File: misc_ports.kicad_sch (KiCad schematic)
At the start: 36 parts, among them J10 Molex 46765-2301, J3 Wuerth_7499010121A, J7 QMTECH JTAG, J8 RTC, J9 1140084168 microSD Card Slot, P1 Full-side CD Card Slot, U12 DP83826, U13 74LVC374, U14 PTN3363BSMP

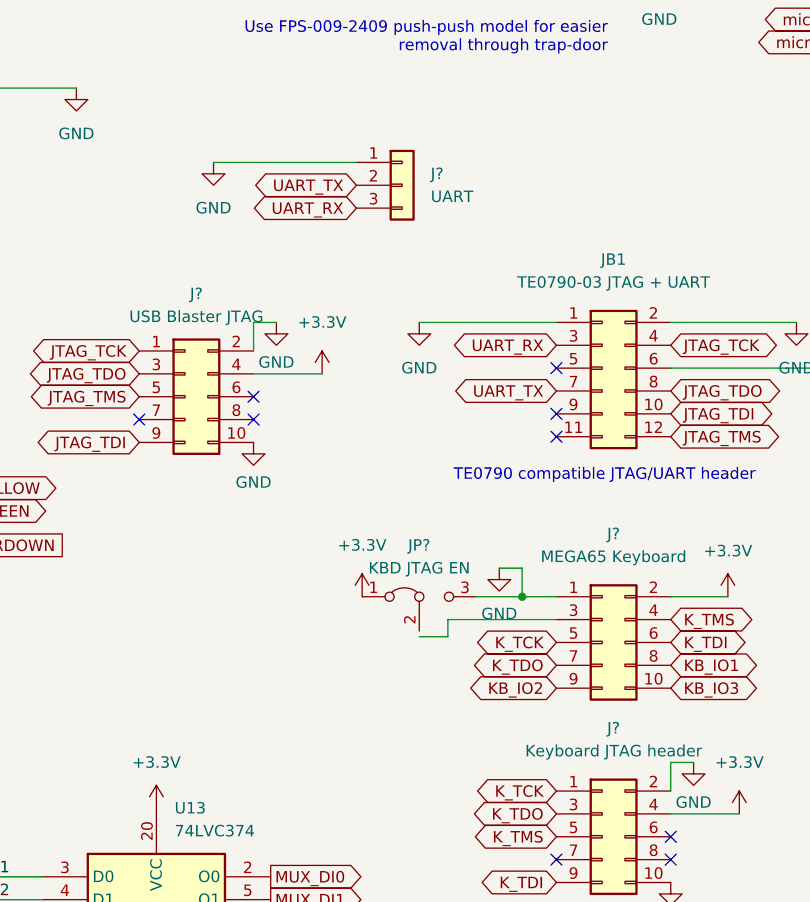
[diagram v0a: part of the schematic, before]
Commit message: place some mounting holes and reset button #3
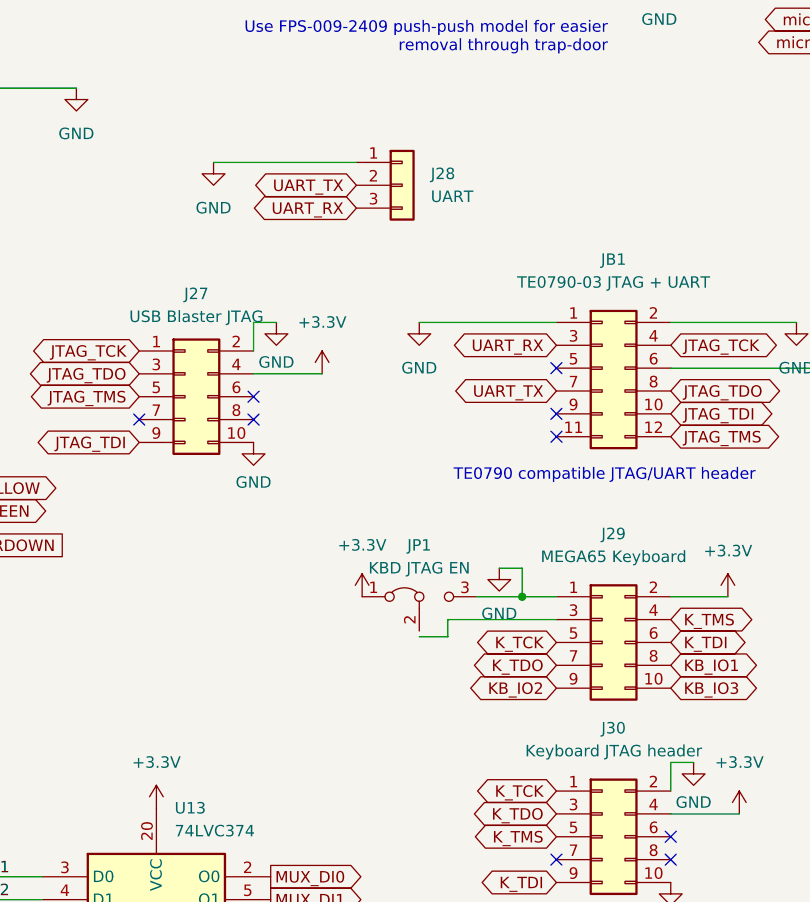
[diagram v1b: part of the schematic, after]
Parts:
- gave numbers to parts that had none: 5
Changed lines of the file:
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@@
   (symbol (lib_id "Connector_Generic:Conn_01x03") (at 128.905 80.645 0) (unit 1)
     (in_bom yes) (on_board yes) (fields_autoplaced)
-    (property "Reference" "J?" (id 0) (at 132.08 79.3749 0)
+    (property "Reference" "J28" (id 0) (at 132.08 79.3749 0)
       (effects (font (size 1.27 1.27)) (justify left))
     )
@@
   (symbol (lib_id "power:GND") (at 112.395 109.22 0) (unit 1)
     (in_bom yes) (on_board yes) (fields_autoplaced)
-    (property "Reference" "#PWR?" (id 0) (at 112.395 115.57 0)
+    (property "Reference" "#PWR0299" (id 0) (at 112.395 115.57 0)
       (effects (font (size 1.27 1.27)) hide)
     )
@@
   (symbol (lib_id "power:+3.3V") (at 165.1 126.365 0) (unit 1)
     (in_bom yes) (on_board yes) (fields_autoplaced)
-    (property "Reference" "#PWR?" (id 0) (at 165.1 130.175 0)
+    (property "Reference" "#PWR0300" (id 0) (at 165.1 130.175 0)
       (effects (font (size 1.27 1.27)) hide)
     )
@@
   (symbol (lib_id "Connector_Generic:Conn_02x05_Odd_Even") (at 151.13 153.035 0) (unit 1)
     (in_bom yes) (on_board yes) (fields_autoplaced)
-    (property "Reference" "J?" (id 0) (at 152.4 140.97 0))
+    (property "Reference" "J30" (id 0) (at 152.4 140.97 0))
     (property "Value" "Keyboard JTAG header" (id 1) (at 152.4 143.51 0))
     (property "Footprint" "Connector_PinHeader_2.54mm:PinHeader_2x05_P2.54mm_Vertical" (id 2) (at 151.13 153.035 0)
@@
   (symbol (lib_id "Connector_Generic:Conn_02x05_Odd_Even") (at 151.13 131.445 0) (unit 1)
     (in_bom yes) (on_board yes) (fields_autoplaced)
-    (property "Reference" "J?" (id 0) (at 152.4 119.38 0))
+    (property "Reference" "J29" (id 0) (at 152.4 119.38 0))
     (property "Value" "MEGA65 Keyboard" (id 1) (at 152.4 121.92 0))
     (property "Footprint" "" (id 2) (at 151.13 131.445 0)
@@
   (symbol (lib_id "Jumper:Jumper_3_Bridged12") (at 130.81 126.365 0) (unit 1)
     (in_bom yes) (on_board yes) (fields_autoplaced)
-    (property "Reference" "JP?" (id 0) (at 130.81 120.65 0))
+    (property "Reference" "JP1" (id 0) (at 130.81 120.65 0))
     (property "Value" "KBD JTAG EN" (id 1) (at 130.81 123.19 0))
     (property "Footprint" "Connector_PinHeader_2.54mm:PinHeader_1x03_P2.54mm_Vertical" (id 2) (at 130.81 126.365 0)
@@
   (symbol (lib_id "power:+3.3V") (at 166.37 150.495 0) (unit 1)
     (in_bom yes) (on_board yes) (fields_autoplaced)
-    (property "Reference" "#PWR?" (id 0) (at 166.37 154.305 0)
+    (property "Reference" "#PWR0303" (id 0) (at 166.37 154.305 0)
       (effects (font (size 1.27 1.27)) hide)
     )
@@
   (symbol (lib_id "Connector_Generic:Conn_02x05_Odd_Even") (at 104.775 104.14 0) (unit 1)
     (in_bom yes) (on_board yes) (fields_autoplaced)
-    (property "Reference" "J?" (id 0) (at 106.045 92.71 0))
+    (property "Reference" "J27" (id 0) (at 106.045 92.71 0))
     (property "Value" "USB Blaster JTAG" (id 1) (at 106.045 95.25 0))
     (property "Footprint" "Connector_PinHeader_2.54mm:PinHeader_2x05_P2.54mm_Vertical" (id 2) (at 104.775 104.14 0)
@@
   (symbol (lib_id "power:GND") (at 161.29 144.78 0) (unit 1)
     (in_bom yes) (on_board yes) (fields_autoplaced)
-    (property "Reference" "#PWR?" (id 0) (at 161.29 151.13 0)
+    (property "Reference" "#PWR0301" (id 0) (at 161.29 151.13 0)
       (effects (font (size 1.27 1.27)) hide)
     )
@@
   (symbol (lib_id "power:GND") (at 114.935 95.885 0) (unit 1)
     (in_bom yes) (on_board yes) (fields_autoplaced)
-    (property "Reference" "#PWR?" (id 0) (at 114.935 102.235 0)
+    (property "Reference" "#PWR0296" (id 0) (at 114.935 102.235 0)
       (effects (font (size 1.27 1.27)) hide)
     )
@@
   (symbol (lib_id "power:GND") (at 107.95 78.105 0) (unit 1)
     (in_bom yes) (on_board yes) (fields_autoplaced)
-    (property "Reference" "#PWR?" (id 0) (at 107.95 84.455 0)
+    (property "Reference" "#PWR0294" (id 0) (at 107.95 84.455 0)
       (effects (font (size 1.27 1.27)) hide)
     )
@@
   (symbol (lib_id "power:+3.3V") (at 124.46 126.365 0) (unit 1)
     (in_bom yes) (on_board yes) (fields_autoplaced)
-    (property "Reference" "#PWR?" (id 0) (at 124.46 130.175 0)
+    (property "Reference" "#PWR0297" (id 0) (at 124.46 130.175 0)
       (effects (font (size 1.27 1.27)) hide)
     )
@@
   (symbol (lib_id "power:+3.3V") (at 120.015 101.6 0) (unit 1)
     (in_bom yes) (on_board yes) (fields_autoplaced)
-    (property "Reference" "#PWR?" (id 0) (at 120.015 105.41 0)
+    (property "Reference" "#PWR0295" (id 0) (at 120.015 105.41 0)
       (effects (font (size 1.27 1.27)) hide)
     )
@@
   (symbol (lib_id "power:GND") (at 158.75 158.115 0) (unit 1)
     (in_bom yes) (on_board yes) (fields_autoplaced)
-    (property "Reference" "#PWR?" (id 0) (at 158.75 164.465 0)
+    (property "Reference" "#PWR0302" (id 0) (at 158.75 164.465 0)
       (effects (font (size 1.27 1.27)) hide)
     )
@@
   (symbol (lib_id "power:GND") (at 139.7 123.19 0) (unit 1)
     (in_bom yes) (on_board yes) (fields_autoplaced)
-    (property "Reference" "#PWR?" (id 0) (at 139.7 129.54 0)
-      (effects (font (size 1.27 1.27)) hide)
-    )
+    (property "Reference" "#PWR0298" (id 0) (at 139.7 129.54 0)
+      (effects (font (size 1.27 1.27)) hide)
+    )

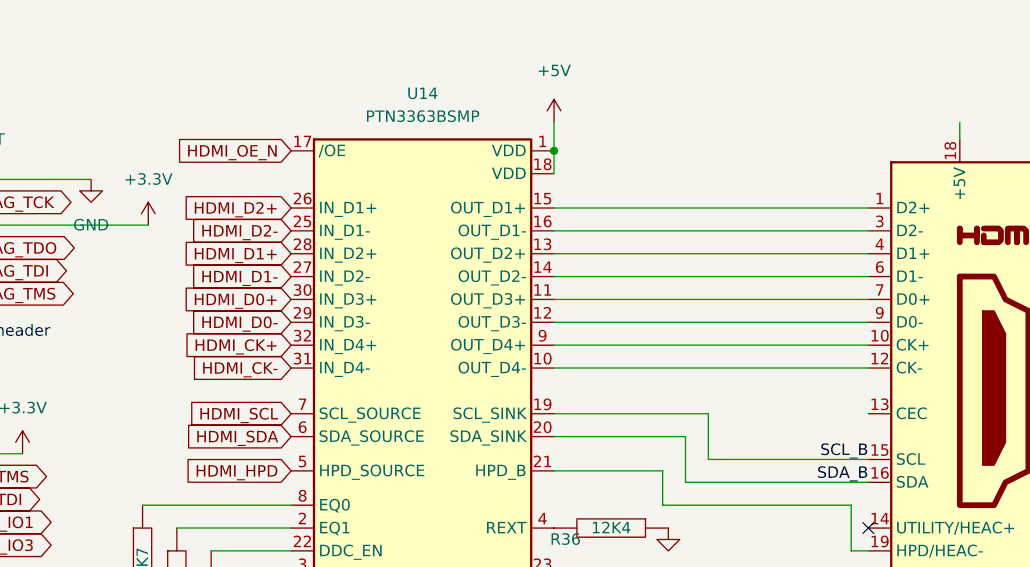
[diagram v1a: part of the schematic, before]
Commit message: rearrange FPGA board connectors to detangle. Begin routing HDMI
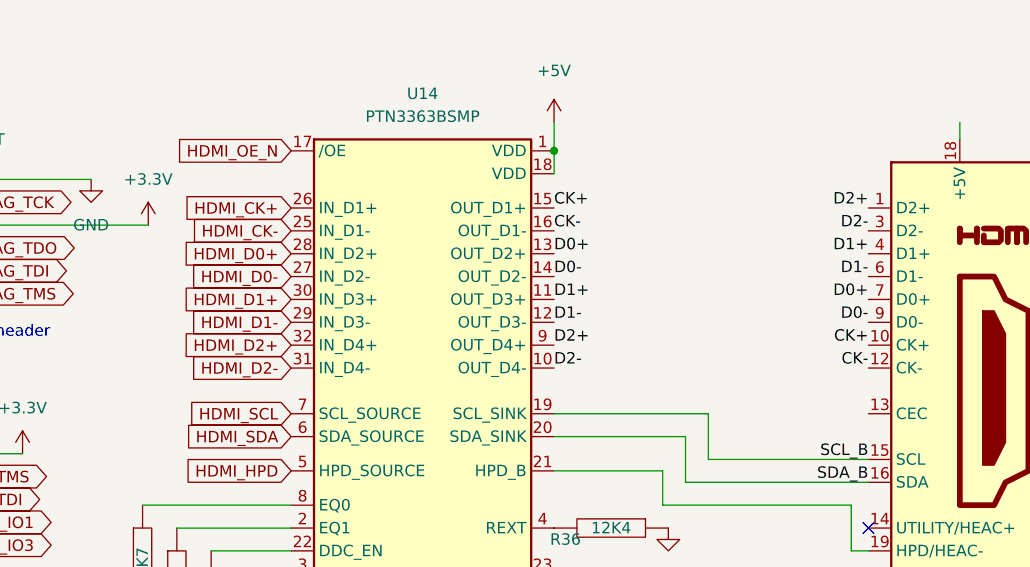
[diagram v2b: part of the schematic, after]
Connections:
- net HDMI_CK+: now also U14.26 (IN_D1+); no longer U14.32 (IN_D4+)
- net HDMI_CK-: now also U14.25 (IN_D1-); no longer U14.31 (IN_D4-)
- net HDMI_D0+: now also U14.28 (IN_D2+); no longer U14.30 (IN_D3+)
- net HDMI_D0-: now also U14.27 (IN_D2-); no longer U14.29 (IN_D3-)
- net HDMI_D1+: now also U14.30 (IN_D3+); no longer U14.28 (IN_D2+)
- net HDMI_D1-: now also U14.29 (IN_D3-); no longer U14.27 (IN_D2-)
- net HDMI_D2+: now also U14.32 (IN_D4+); no longer U14.26 (IN_D1+)
- net HDMI_D2-: now also U14.31 (IN_D4-); no longer U14.25 (IN_D1-)
- net CK+: now reaches U14.15 (OUT_D1+)
- net CK+: now also J10.10 (CK+); no longer J10.1 (D2+)
- net D2+: now reaches U14.9 (OUT_D4+)
- net D2+: now also J10.1 (D2+); no longer J10.10 (CK+)
- net CK-: now reaches J10.12 (CK-)
- net CK-: now also U14.16 (OUT_D1-); no longer U14.10 (OUT_D4-)
- net D2-: now reaches J10.3 (D2-)
- net D2-: now also U14.10 (OUT_D4-); no longer U14.16 (OUT_D1-)
- net D0+: now reaches U14.13 (OUT_D2+)
- net D0+: now also J10.7 (D0+); no longer J10.4 (D1+)
- net D0-: now reaches U14.14 (OUT_D2-)
- net D0-: now also J10.9 (D0-); no longer J10.6 (D1-)
- net D1+: now reaches U14.11 (OUT_D3+)
- net D1+: now also J10.4 (D1+); no longer J10.7 (D0+)
- net D1-: now reaches U14.12 (OUT_D3-)
- net D1-: now also J10.6 (D1-); no longer J10.9 (D0-)

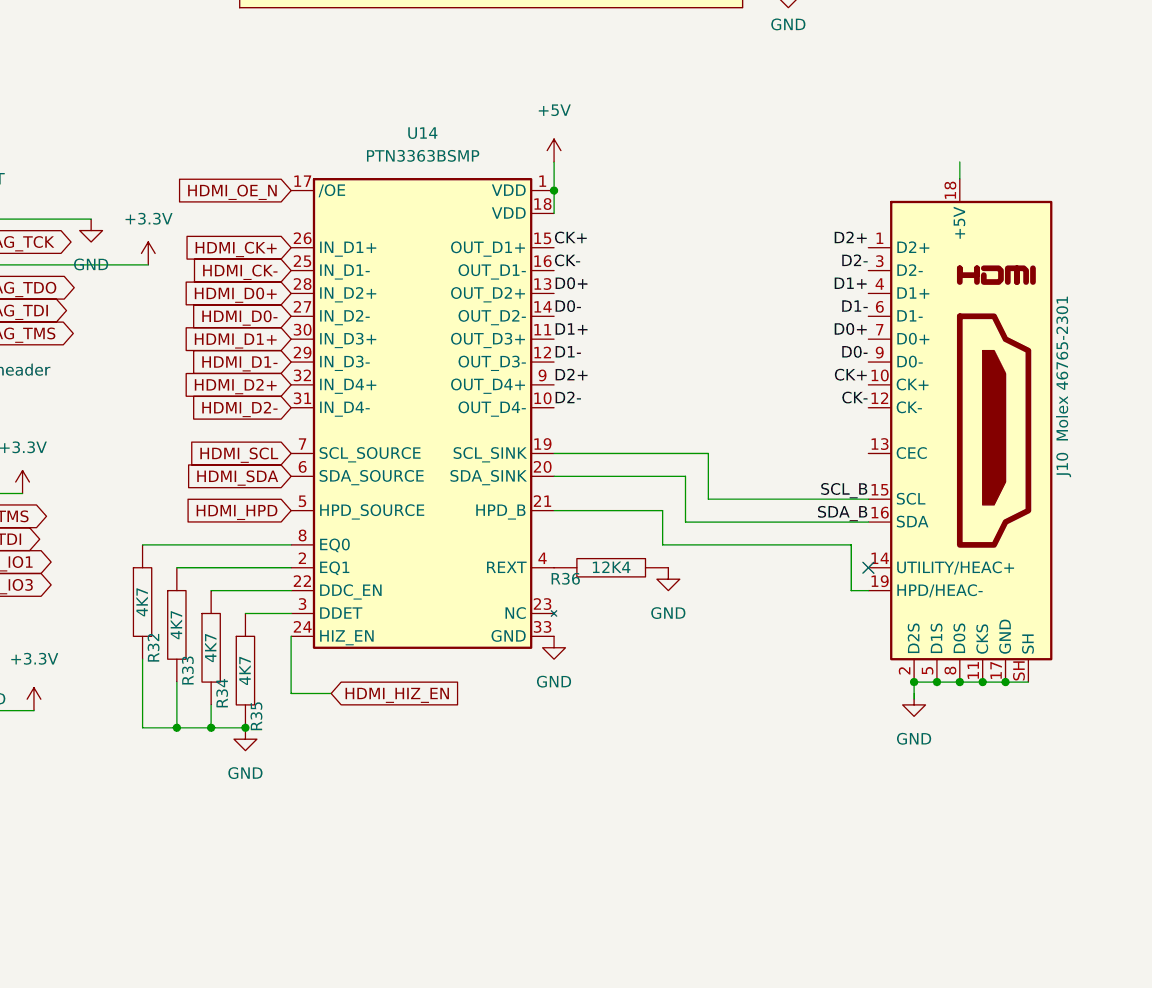
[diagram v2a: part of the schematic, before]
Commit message: Replace HDMI connector #13
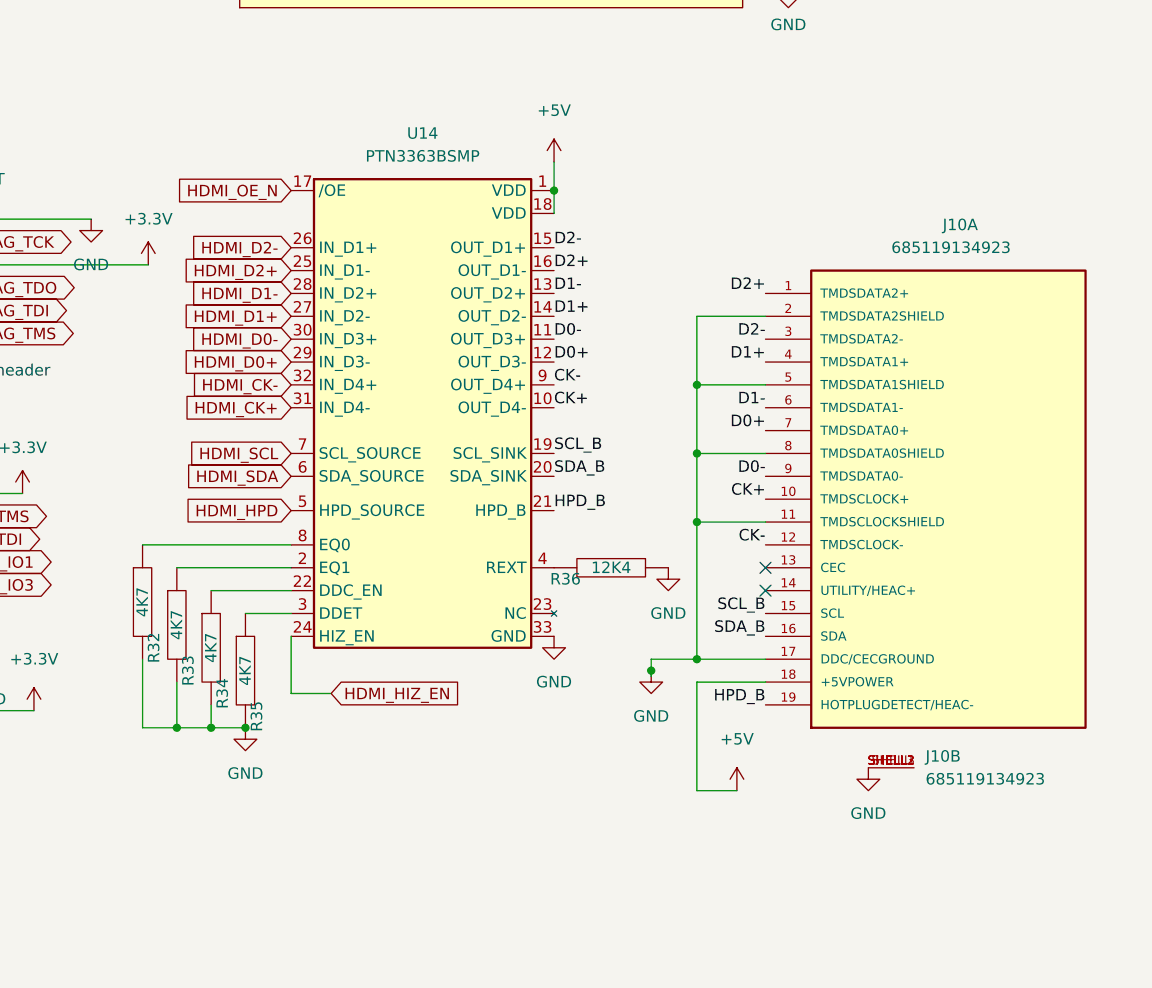
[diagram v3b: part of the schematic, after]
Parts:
- removed J10: Molex 46765-2301, Connector_HDMI:HDMI_A_Contact_Technology_HDMI-19APL2_Horizontal, symbol Connector:HDMI_A_1.4
- added J10: 685119134923, 685119134923, symbol 00ProjectHDMI:685119134923
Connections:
- net +5V: now also J10.18 (+5VPOWER)
- net CK+: now also U14.10 (OUT_D4-), J10.10 (TMDSCLOCK+); no longer U14.15 (OUT_D1+)
- net CK-: now also U14.9 (OUT_D4+), J10.12 (TMDSCLOCK-); no longer U14.16 (OUT_D1-)
- net D0+: now also U14.12 (OUT_D3-), J10.7 (TMDSDATA0+); no longer U14.13 (OUT_D2+)
- net D0-: now also U14.11 (OUT_D3+), J10.9 (TMDSDATA0-); no longer U14.14 (OUT_D2-)
- net D1+: now also U14.14 (OUT_D2-), J10.4 (TMDSDATA1+); no longer U14.11 (OUT_D3+)
- net D1-: now also U14.13 (OUT_D2+), J10.6 (TMDSDATA1-); no longer U14.12 (OUT_D3-)
- net D2+: now also U14.16 (OUT_D1-), J10.1 (TMDSDATA2+); no longer U14.9 (OUT_D4+)
- net D2-: now also U14.15 (OUT_D1+), J10.3 (TMDSDATA2-); no longer U14.10 (OUT_D4-)
- net GND: now also J10.11 (TMDSCLOCKSHIELD), J10.17 (DDC/CECGROUND), J10.2 (TMDSDATA2SHIELD), J10.5 (TMDSDATA1SHIELD), J10.8 (TMDSDATA0SHIELD), J10.SHELL, J10.SHELL1, J10.SHELL2, J10.SHELL3
- net HDMI_CK+: now also U14.31 (IN_D4-); no longer U14.26 (IN_D1+)
- net HDMI_CK-: now also U14.32 (IN_D4+); no longer U14.25 (IN_D1-)
- net HDMI_D0+: now also U14.29 (IN_D3-); no longer U14.28 (IN_D2+)
- net HDMI_D0-: now also U14.30 (IN_D3+); no longer U14.27 (IN_D2-)
- net HDMI_D1+: now also U14.27 (IN_D2-); no longer U14.30 (IN_D3+)
- net HDMI_D1-: now also U14.28 (IN_D2+); no longer U14.29 (IN_D3-)
- net HDMI_D2+: now also U14.25 (IN_D1-); no longer U14.32 (IN_D4+)
- net HDMI_D2-: now also U14.26 (IN_D1+); no longer U14.31 (IN_D4-)
- net SCL_B: now also J10.15 (SCL)
- net SDA_B: now also J10.16 (SDA)
- net HPD_B: now reaches U14.21 (HPD_B)
- net HPD_B: now also J10.19 (HOTPLUGDETECT/HEAC-)
- no-connect marks 17 -> 18

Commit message: add missing footprints
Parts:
- J29: footprint (none) -> Connector_PinHeader_2.54mm:PinHeader_2x05_P2.54mm_Vertical
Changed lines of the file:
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@@
     (property "Reference" "J29" (id 0) (at 152.4 119.38 0))
     (property "Value" "MEGA65 Keyboard" (id 1) (at 152.4 121.92 0))
-    (property "Footprint" "" (id 2) (at 151.13 131.445 0)
+    (property "Footprint" "Connector_PinHeader_2.54mm:PinHeader_2x05_P2.54mm_Vertical" (id 2) (at 151.13 131.445 0)
       (effects (font (size 1.27 1.27)) hide)
     )

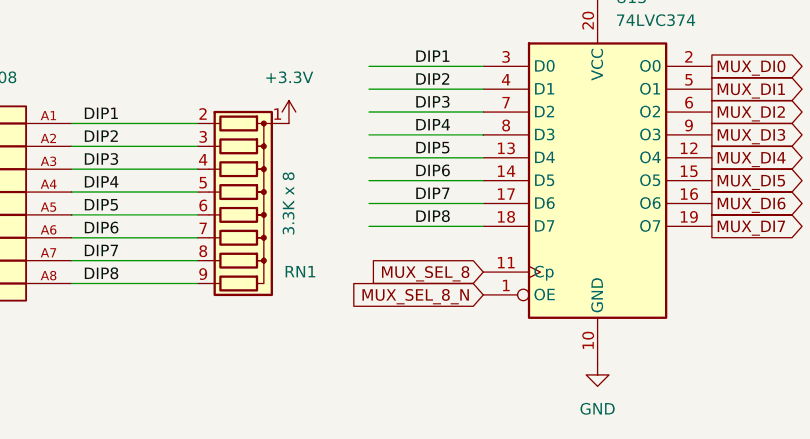
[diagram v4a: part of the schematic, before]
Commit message: renumber MUX registers to ease routing
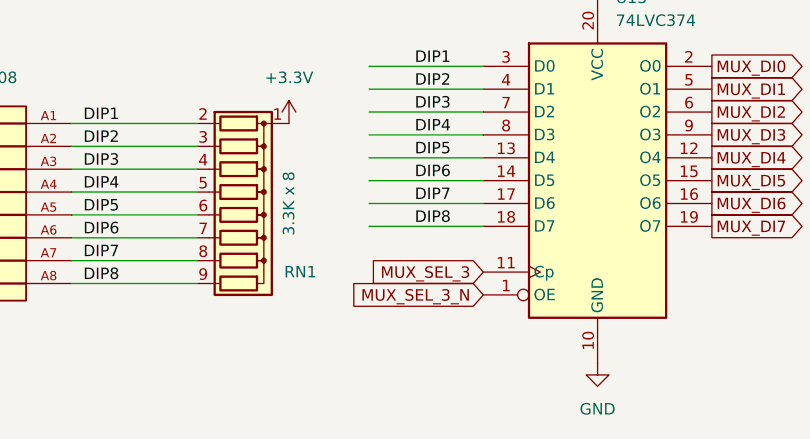
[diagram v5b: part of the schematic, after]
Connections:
- net MUX_SEL_8 renamed MUX_SEL_3
- net MUX_SEL_8_N renamed MUX_SEL_3_N
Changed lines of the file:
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@@
     )
   )
-  (global_label "MUX_SEL_8" (shape input) (at 88.9 180.34 180) (fields_autoplaced)
+  (global_label "MUX_SEL_3" (shape input) (at 88.9 180.34 180) (fields_autoplaced)
     (effects (font (size 1.27 1.27)) (justify right))
     (property "Intersheet References" "${INTERSHEET_REFS}" (id 0) (at 75.964 180.2606 0)
@@
     )
   )
-  (global_label "MUX_SEL_8_N" (shape input) (at 88.9 182.88 180) (fields_autoplaced)
+  (global_label "MUX_SEL_3_N" (shape input) (at 88.9 182.88 180) (fields_autoplaced)
     (effects (font (size 1.27 1.27)) (justify right))
     (property "Intersheet References" "${INTERSHEET_REFS}" (id 0) (at 73.6659 182.8006 0)
